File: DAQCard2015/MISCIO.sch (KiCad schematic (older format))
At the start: 12 parts, among them P3 miniDIL20, P4 LEMO_EPY.00.250.NTN, P5 LEMO_EPY.00.250.NTN, P6 FAN, Q1 Q_NPN_BCE, U24 MCP65R41

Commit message: LVDS pins assigned and first round routing finished, work on 3d models
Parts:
- P6: footprint (none) -> Socket_Strips:Socket_Strip_Straight_1x02
- Q1: footprint (none) -> Housings_SOT-23_SOT-143_TSOT-6:SOT-23
- R53, R54, R56, TH1: footprint (none) -> Resistors_SMD:R_0603
- R55: footprint (none) -> Resistors_SMD:R_0805
- RV1: footprint (none) -> extras:SM31TW+0805
- U24: footprint (none) -> Housings_SOT-23_SOT-143_TSOT-6:SOT-23-6
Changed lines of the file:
@@
 F 0 "R53" V 8180 4350 50  0000 C CNN
 F 1 "10k" V 8100 4350 50  0000 C CNN
-F 2 "" V 8030 4350 30  0000 C CNN
+F 2 "Resistors_SMD:R_0603" V 8030 4350 30  0001 C CNN
 F 3 "" H 8100 4350 30  0000 C CNN
 	1    8100 4350
@@
 F 0 "R54" V 8680 4350 50  0000 C CNN
 F 1 "10k" V 8600 4350 50  0000 C CNN
-F 2 "" V 8530 4350 30  0000 C CNN
+F 2 "Resistors_SMD:R_0603" V 8530 4350 30  0001 C CNN
 F 3 "" H 8600 4350 30  0000 C CNN
 	1    8600 4350
@@
 F 0 "RV1" H 8100 5050 50  0000 C CNN
 F 1 "10k" H 8100 5150 50  0000 C CNN
-F 2 "" H 8100 5150 60  0000 C CNN
+F 2 "extras:SM31TW+0805" H 8100 5150 60  0001 C CNN
 F 3 "" H 8100 5150 60  0000 C CNN
 	1    8100 5150
@@
 F 0 "U24" H 9150 4650 40  0000 C CNN
 F 1 "MCP65R41" H 9500 4550 40  0000 C CNN
-F 2 "" H 9100 4650 60  0000 C CNN
+F 2 "Housings_SOT-23_SOT-143_TSOT-6:SOT-23-6" H 9100 4650 60  0001 C CNN
 F 3 "" H 9100 4650 60  0000 C CNN
 	1    9100 4650
@@
 F 0 "TH1" V 8700 5100 50  0000 C CNN
 F 1 "10k Thermistor" V 8500 5050 50  0000 C BNN
-F 2 "" H 8600 5050 60  0000 C CNN
+F 2 "Resistors_SMD:R_0603" H 8600 5050 60  0001 C CNN
 F 3 "" H 8600 5050 60  0000 C CNN
 	1    8600 5050
@@
 	8600 4500 8600 4800
 $Comp
-L GND #PWR1
+L GND #PWR01
 U 1 1 55F022ED
 P 8100 5400
-F 0 "#PWR1" H 8100 5150 50  0001 C CNN
+F 0 "#PWR01" H 8100 5150 50  0001 C CNN
 F 1 "GND" H 8100 5250 50  0000 C CNN
 F 2 "" H 8100 5400 60  0000 C CNN
@@
 $EndComp
 $Comp
-L GND #PWR2
+L GND #PWR02
 U 1 1 55F02317
 P 8600 5300
-F 0 "#PWR2" H 8600 5050 50  0001 C CNN
+F 0 "#PWR02" H 8600 5050 50  0001 C CNN
 F 1 "GND" H 8600 5150 50  0000 C CNN
 F 2 "" H 8600 5300 60  0000 C CNN
@@
 F 0 "Q1" H 10500 4700 50  0000 R CNN
 F 1 "Q_NPN_BCE" H 10800 4600 50  0000 R CNN
-F 2 "" H 10400 4750 29  0000 C CNN
+F 2 "Housings_SOT-23_SOT-143_TSOT-6:SOT-23" H 10400 4750 29  0001 C CNN
 F 3 "" H 10200 4650 60  0000 C CNN
 	1    10200 4650
@@
 F 0 "R56" V 9830 4650 50  0000 C CNN
 F 1 "253R" V 9750 4650 50  0000 C CNN
-F 2 "" V 9680 4650 30  0000 C CNN
+F 2 "Resistors_SMD:R_0603" V 9680 4650 30  0001 C CNN
 F 3 "" H 9750 4650 30  0000 C CNN
 	1    9750 4650
@@
 F 0 "P6" H 10500 4400 50  0000 C CNN
 F 1 "FAN" V 10600 4250 50  0000 C CNN
-F 2 "" H 10500 4250 60  0000 C CNN
+F 2 "Socket_Strips:Socket_Strip_Straight_1x02" H 10500 4250 60  0001 C CNN
 F 3 "" H 10500 4250 60  0000 C CNN
 	1    10500 4250
@@
 F 0 "R55" V 9130 4950 50  0000 C CNN
 F 1 "50k" V 9050 4950 50  0000 C CNN
-F 2 "" V 8980 4950 30  0000 C CNN
+F 2 "Resistors_SMD:R_0805" V 8980 4950 30  0001 C CNN
 F 3 "" H 9050 4950 30  0000 C CNN
 	1    9050 4950

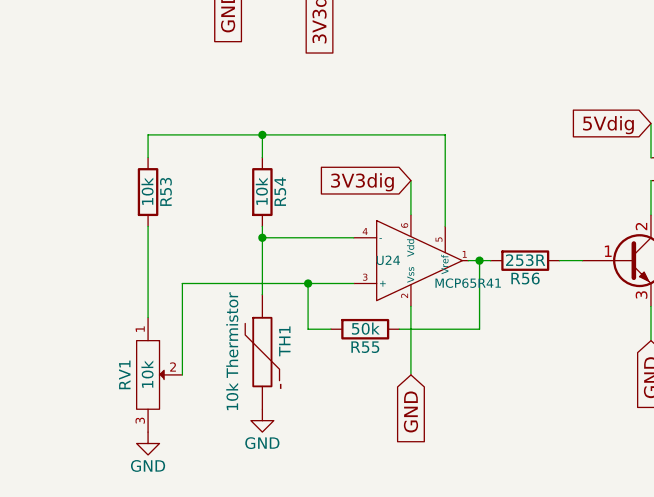
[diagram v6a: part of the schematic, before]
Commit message: Reroutes LVDS signals to give pairs proper impedances
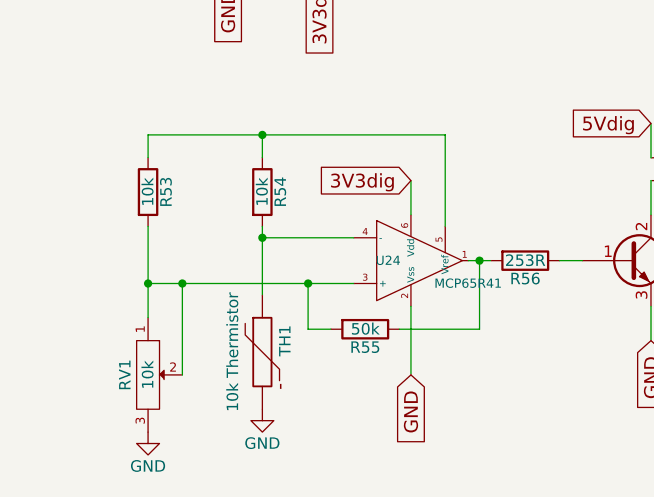
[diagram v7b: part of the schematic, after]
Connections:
- net at R53.2, RV1.1: now also R55.2, RV1.2, U24.3 (+)
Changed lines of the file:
@@
 	8250 5150 8250 4750
 Wire Wire Line
-	8250 4750 9000 4750
+	8100 4750 9000 4750
 Wire Wire Line
 	8100 4900 8100 4500
@@
 	8800 4950 8800 4750
 Connection ~ 8800 4750
+Connection ~ 8100 4750
+Connection ~ 8250 4750
 $EndSCHEMATC

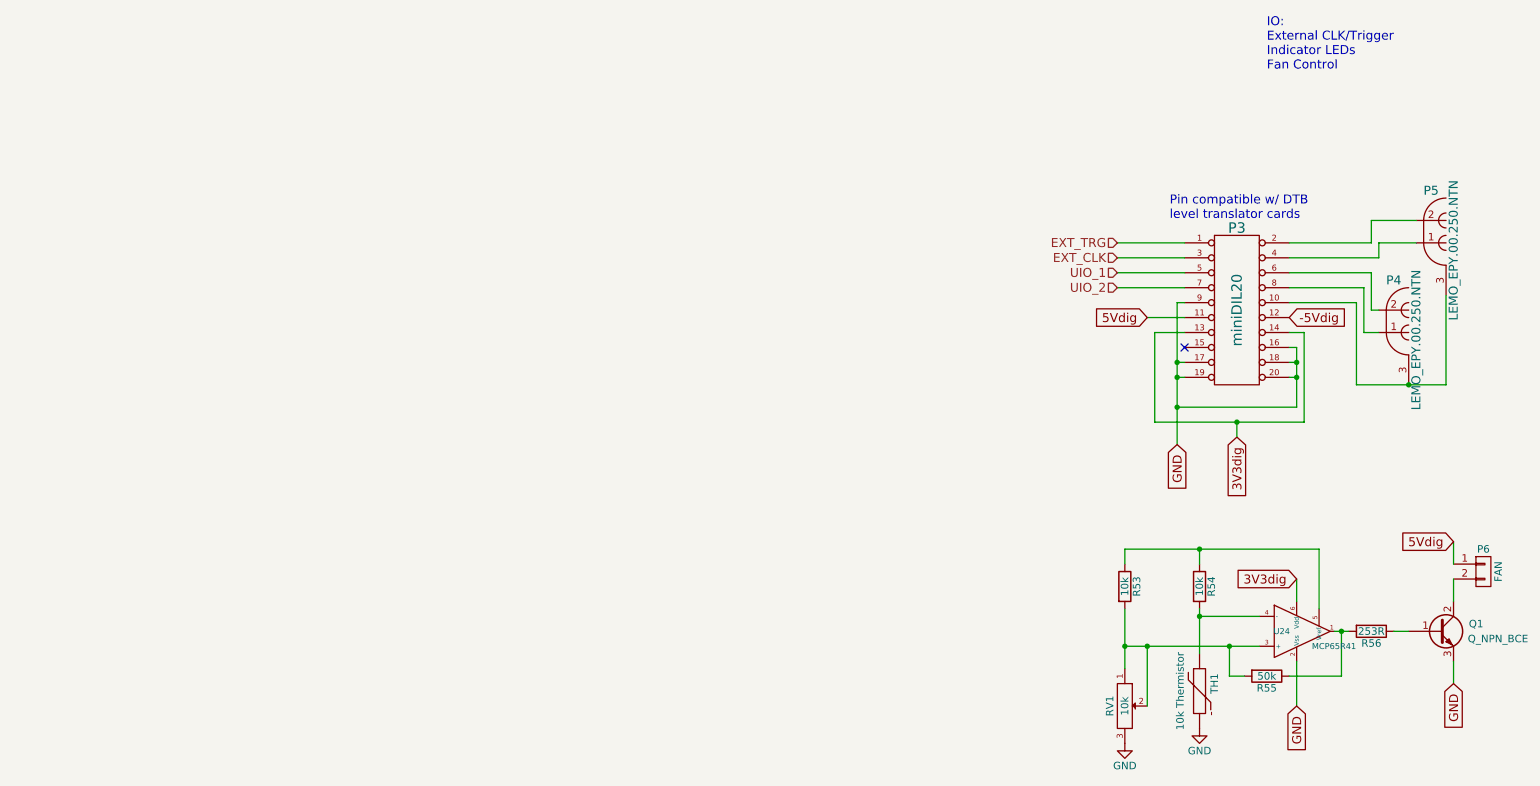
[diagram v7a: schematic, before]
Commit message: Updates to DAQ system including adjusting position of ZEM and adding Control signal outputs
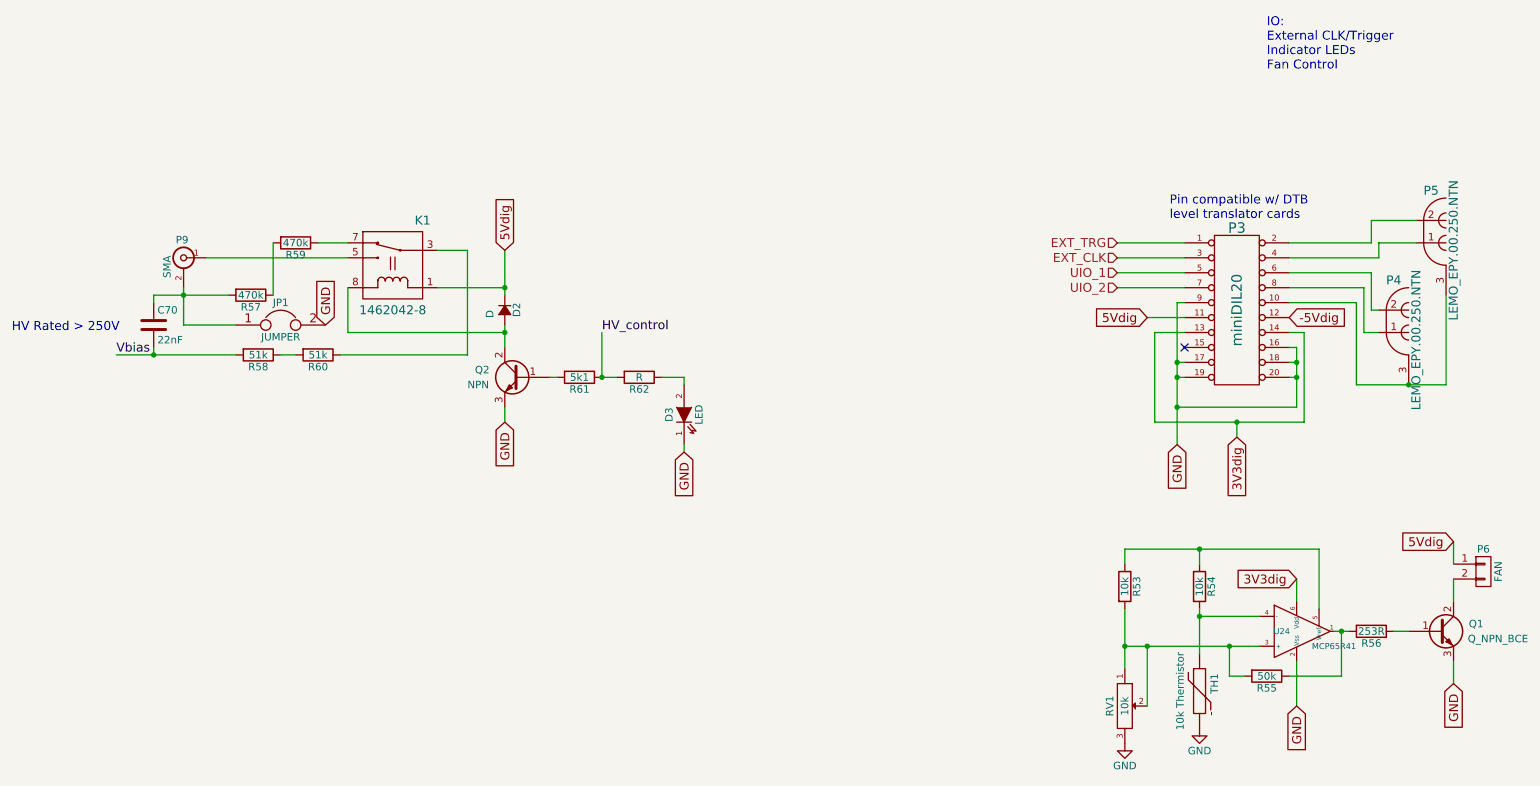
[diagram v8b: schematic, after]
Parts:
- added C70: 22nF, symbol C
- added D2: D, symbol D_Small
- added D3: LED, symbol LED
- added JP1: JUMPER, symbol JUMPER
- added K1: 1462042-8, symbol relaySPDT
- added P9: SMA, symbol BNC
- added Q2: NPN, symbol Q_NPN_BCE
- added R57, R59: 470k, symbol R
- added R58, R60: 51k, symbol R
- added R61: 5k1, symbol R
- added R62: R, symbol R
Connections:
- net 5Vdig: now also D2.1 (K), K1.1
- net GND: now also D3.1 (K), JP1.2, Q2.3 (E)
- new net: K1.3, R60.1
- new net: K1.5, P9.1 (In)
- new net: K1.7, R59.1
- new net: D2.2 (A), K1.8, Q2.2 (C)
- new net: R57.1, R59.2
- new net: C70.1, JP1.1, P9.2 (Ext), R57.2
- new net: R58.1, R60.2
- new net: Q2.1 (B), R61.2
- new net: D3.2 (A), R62.1
- new net HV_control: R61.1, R62.2
- new net Vbias: C70.2, R58.2
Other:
- note added: "HV Rated > 250V"
